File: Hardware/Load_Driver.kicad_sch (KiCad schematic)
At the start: 4 parts

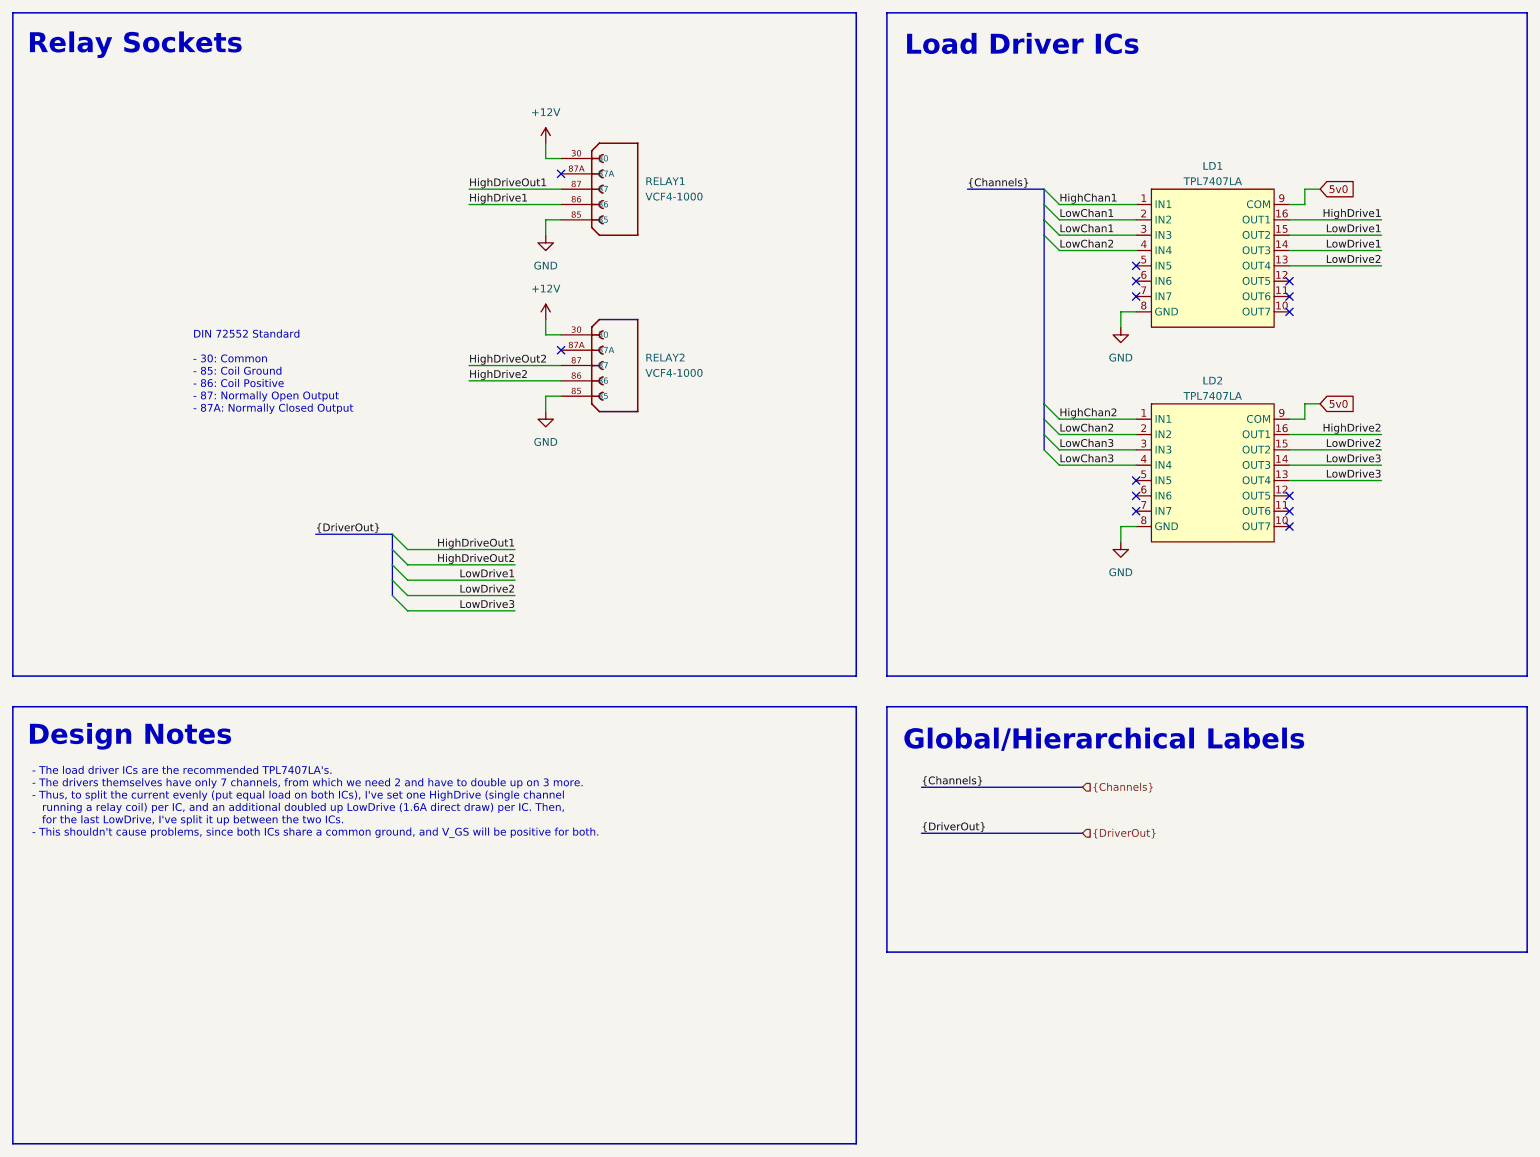
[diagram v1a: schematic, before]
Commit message: Replaced G0B1KET6 with KET6N in schematic
- Updated the schematic with new symbol and pinout.
- Updated the rest of the schematic with all resulting changes
	- This includes the 8 output channels, 7 GPIOs, and slightly
	  different WAGO connector configuration.
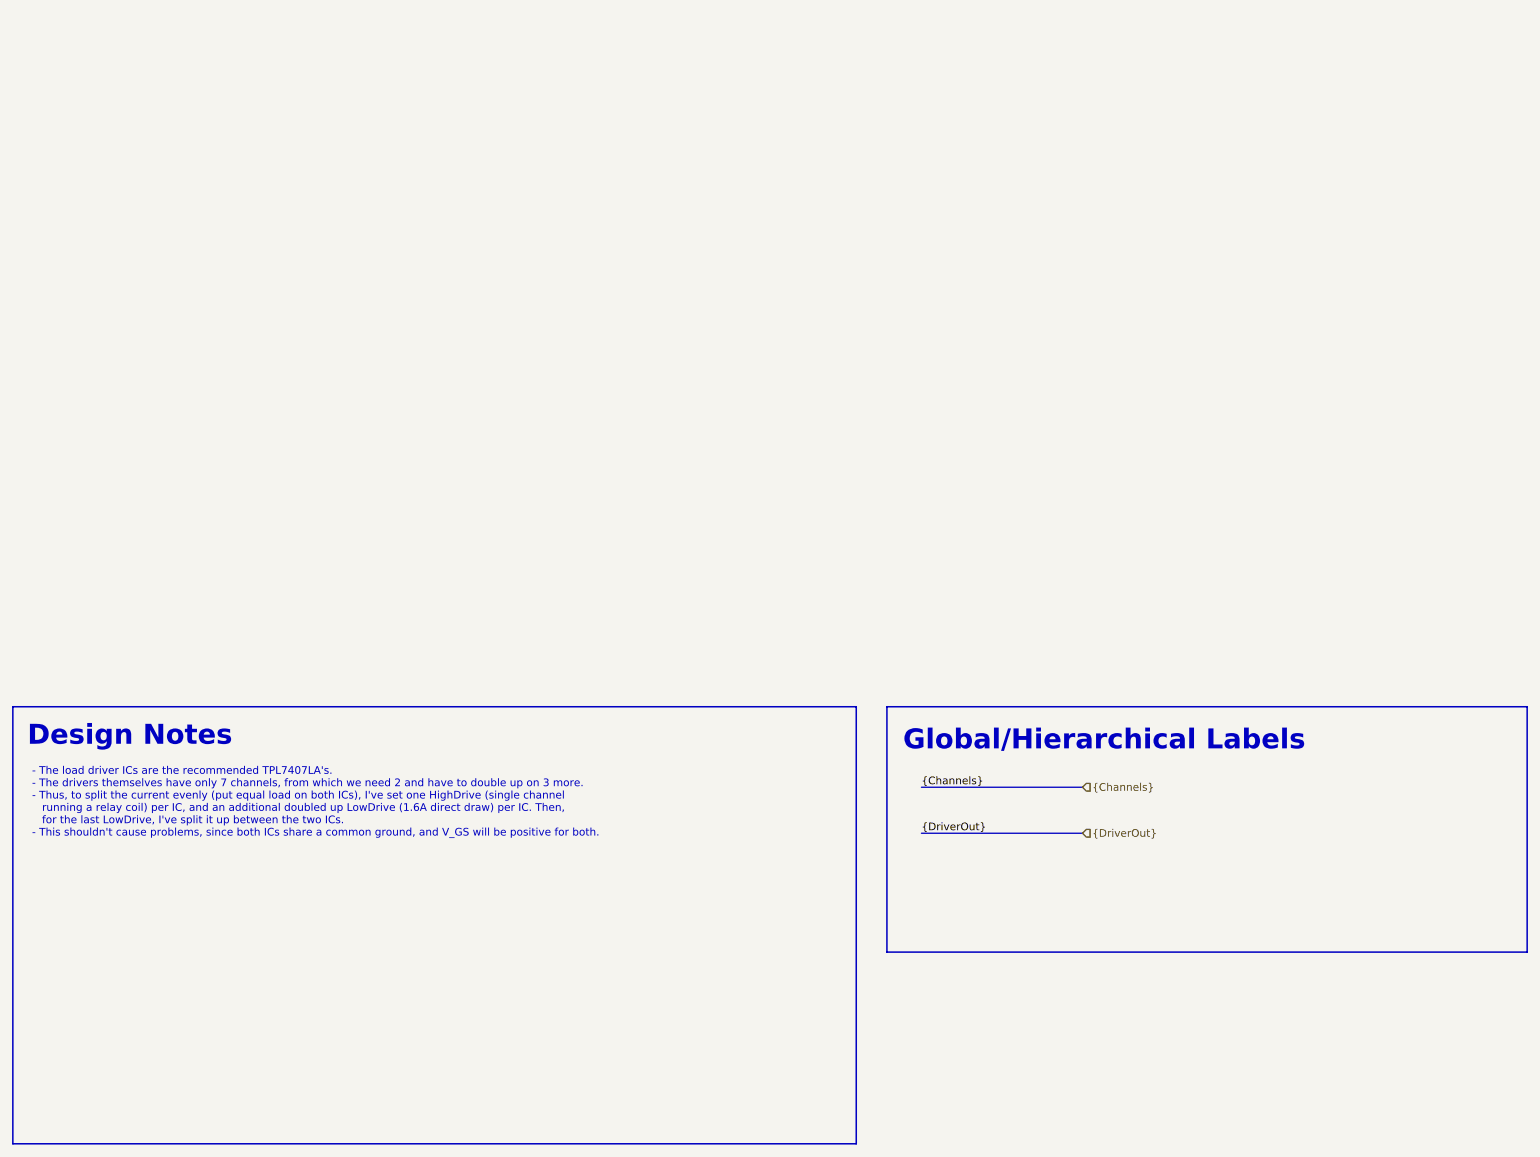
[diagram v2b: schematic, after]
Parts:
- removed LD1, LD2: TPL7407LA, Package_SO:SOIC-16_3.9x9.9mm_P1.27mm, symbol symbols:TPL7407LA
- removed RELAY1, RELAY2: VCF4-1000, footprints:TE_VCF4-1000, symbol symbols:VCF4-1000
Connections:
- no-connect marks 14 -> 0
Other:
- note removed: "DIN 72552 Standard - 30: Common - 85: Coil Ground - 86: Coil Positive - 87: Normally Open Output - 87A: Normally Closed Output"
- note removed: "Load Driver ICs"
- note removed: "Relay Sockets"

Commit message: Finished the board
- Board layout and routing is finished. Need to fix ~30 ERC errors and
  add thorough notes throughout, but otherwise that's it.
- Once ERC errors are resolved, will post BOM and Gerbers as a release.
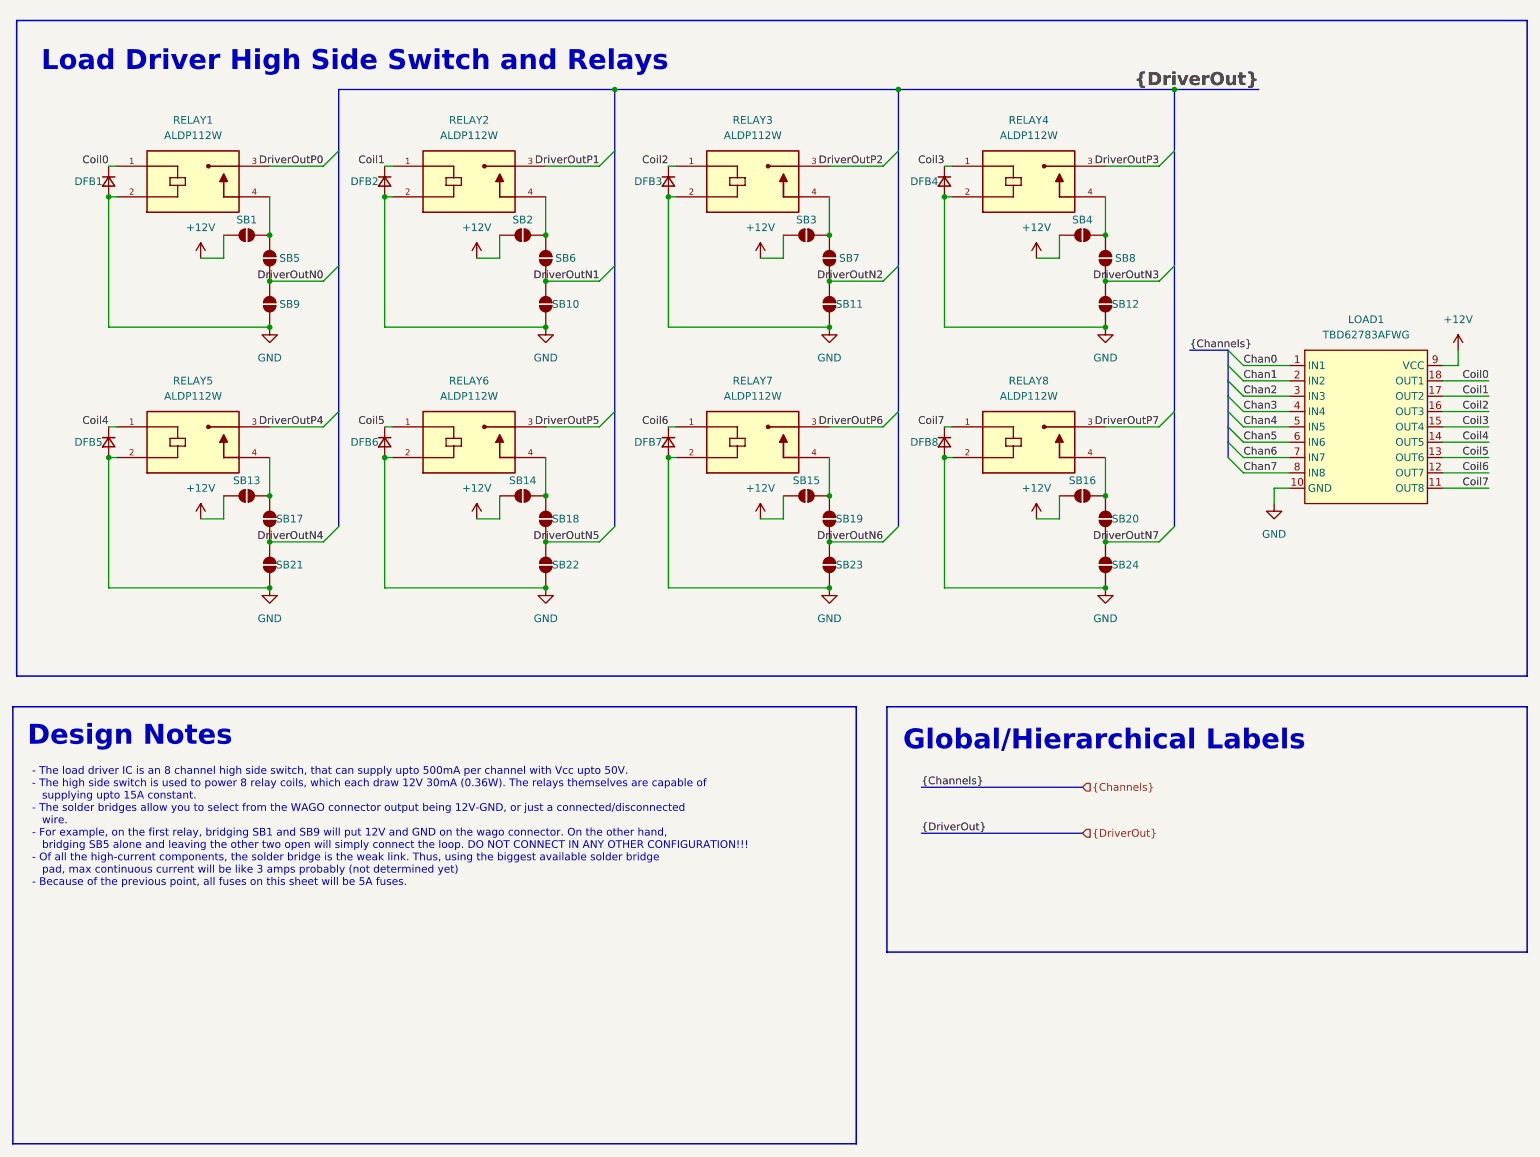
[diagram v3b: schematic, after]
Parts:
- added DFB1, DFB2, DFB3, DFB4, DFB5, DFB6, DFB7, DFB8: D_Small, Diode_THT:D_DO-35_SOD27_P7.62mm_Horizontal, symbol Device:D_Small
- added LOAD1: TBD62783AFWG, Package_SO:SOP-18_7x12.5mm_P1.27mm, symbol symbols:TBD62783AFWG
- added RELAY1, RELAY2, RELAY3, RELAY4, RELAY5, RELAY6, RELAY7, RELAY8: ALDP112W, footprints:RELAY_ALDP112W, symbol symbols:ALDP112W
- added SB1, SB10, SB11, SB12, SB13, SB14, SB15, SB16, SB17, SB18, SB19, SB2, SB20, SB21, SB22, SB23, SB24, SB3, SB4, SB5, SB6, SB7, SB8, SB9: SolderJumper_2_Open, Jumper:SolderJumper-2_P1.3mm_Open_TrianglePad1.0x1.5mm, symbol Jumper:SolderJumper_2_Open
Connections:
- new net: RELAY1.4, SB1.2 (B), SB5.1 (A)
- new net: RELAY5.4, SB13.2 (B), SB17.1 (A)
- new net: RELAY3.4, SB3.2 (B), SB7.1 (A)
- new net: RELAY7.4, SB15.2 (B), SB19.1 (A)
- new net: RELAY8.4, SB16.2 (B), SB20.1 (A)
- new net: RELAY2.4, SB2.2 (B), SB6.1 (A)
- new net: RELAY6.4, SB14.2 (B), SB18.1 (A)
- new net: RELAY4.4, SB4.2 (B), SB8.1 (A)
- new net +12V: LOAD1.9 (VCC), SB1.1 (A), SB13.1 (A), SB14.1 (A), SB15.1 (A), SB16.1 (A), SB2.1 (A), SB3.1 (A), SB4.1 (A)
- new net Chan0: LOAD1.1 (IN1)
- new net Chan1: LOAD1.2 (IN2)
- new net Chan2: LOAD1.3 (IN3)
- new net Chan3: LOAD1.4 (IN4)
- new net Chan4: LOAD1.5 (IN5)
- new net Chan5: LOAD1.6 (IN6)
- new net Chan6: LOAD1.7 (IN7)
- new net Chan7: LOAD1.8 (IN8)
- new net Coil0: DFB1.1 (K), LOAD1.18 (OUT1), RELAY1.1
- new net Coil1: DFB2.1 (K), LOAD1.17 (OUT2), RELAY2.1
- new net Coil2: DFB3.1 (K), LOAD1.16 (OUT3), RELAY3.1
- new net Coil3: DFB4.1 (K), LOAD1.15 (OUT4), RELAY4.1
- new net Coil4: DFB5.1 (K), LOAD1.14 (OUT5), RELAY5.1
- new net Coil5: DFB6.1 (K), LOAD1.13 (OUT6), RELAY6.1
- new net Coil6: DFB7.1 (K), LOAD1.12 (OUT7), RELAY7.1
- new net Coil7: DFB8.1 (K), LOAD1.11 (OUT8), RELAY8.1
- new net DriverOutN0: SB5.2 (B), SB9.1 (A)
- new net DriverOutN1: SB10.1 (A), SB6.2 (B)
- new net DriverOutN2: SB11.1 (A), SB7.2 (B)
- new net DriverOutN3: SB12.1 (A), SB8.2 (B)
- new net DriverOutN4: SB17.2 (B), SB21.1 (A)
- new net DriverOutN5: SB18.2 (B), SB22.1 (A)
- new net DriverOutN6: SB19.2 (B), SB23.1 (A)
- new net DriverOutN7: SB20.2 (B), SB24.1 (A)
- new net DriverOutP0: RELAY1.3
- new net DriverOutP1: RELAY2.3
- new net DriverOutP2: RELAY3.3
- new net DriverOutP3: RELAY4.3
- new net DriverOutP4: RELAY5.3
- new net DriverOutP5: RELAY6.3
- new net DriverOutP6: RELAY7.3
- new net DriverOutP7: RELAY8.3
- new net GND: DFB1.2 (A), DFB2.2 (A), DFB3.2 (A), DFB4.2 (A), DFB5.2 (A), DFB6.2 (A), DFB7.2 (A), DFB8.2 (A), LOAD1.10 (GND), RELAY1.2, RELAY2.2, RELAY3.2, RELAY4.2, RELAY5.2, RELAY6.2, RELAY7.2, RELAY8.2, SB10.2 (B), SB11.2 (B), SB12.2 (B), SB21.2 (B), SB22.2 (B), SB23.2 (B), SB24.2 (B), SB9.2 (B)
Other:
- note added: "- The load driver IC is an 8 channel high side switch, that can supply upto 500mA per channel with Vcc upto 50V. - The high side switch is used to power 8 relay coils, which each draw 12V 30mA (0.36W). The relays themselves are capable of supplying upto 15A constant. - The solder bridges allow you to select from the WAGO connector output being 12V-GND, or just a connected/disconnected wire. - For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"
- note added: "Load Driver High Side Switch and Relays"
- note removed: "- The load driver ICs are the recommended TPL7407LA's. - The drivers themselves have only 7 channels, from which we need 2 and have to double up on 3 more. - Thus, to split the current evenly (put equal load on both ICs), I've set one HighDrive (single channel running a relay coil) per IC, and an additional doubled up LowDrive (1.6A direct draw) per IC. Then, for the last LowDrive, I've split it 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"
